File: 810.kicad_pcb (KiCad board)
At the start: 2 copper layers, 148 x 105.1 mm, 289 parts, among them J1 PJ301BM, J10 PJ301BM, J11 PJ301BM, J12 PJ301BM, J13 PJ301BM, J14 PJ301BM, J15 JACK_MONO_SW, J16 PJ301BM, J17 PJ301B, J18 PJ301B, J2 PJ301BM, J3 PJ301BM, J4 PJ301B, J5 PJ301B, J6 PJ301BM, J7 PJ301BM, J8 PJ301BM, J9 PJ301BM, P1 CONN_01X08, P2 CONN_02X05, Q1 PMBT2369, Q10 2SK208-GR, Q11 2SC4738, Q12 2SA1832, Q13 2SA1832, Q14 2SA1832, Q2 2SK208-GR, Q3 2SA1618, Q4 2SC4207, Q5 2SK208-GR, Q6 MMBF4391LT1G, Q7 2SA1832, Q8 PMBT2369, Q9 2SK208-GR, SW1 DP6T-QY-25S-A, SW1 SPDT, SW2 SPDT, SW3 BF3-1050, U1 TL072-, U10 RC4558, U11 TL074-, U12 TA75S558F, U13 TA75S558F, U14 TA75S558F, U15 TA75S558F, U16 TA75S558F, U17 CD4052, U18 TA75S558F, U2 TL072-, U3 TL072-, U4 CD40106, U5 CD4027, U6 LM13700, U7 LM13700, U8 LM13700, U9 TL072-

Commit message: added hard/soft sync switch
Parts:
- added P3: CONN_01X03, Pin_Headers:Pin_Header_Straight_1x03_Pitch2.54mm, F.Cu at (158.0, 161.2)
- added P4: CONN_01X08, Pin_Headers:Pin_Header_Angled_1x08_Pitch2.54mm, B.Cu at (104.8, 79.8)
- added R135: 15K, MyModules:SM0603-R-JRL, F.Cu at (158.0, 161.2)
- added SW4: SPDT, MyModules:SS-12F108-1P2T-SLIDE, F.Cu at (158.0, 161.2)
- C45, C46, D17, D18, F1, F2, P2: moved to B.Cu
- moved F1 111.9 mm to (223.2, 70.2), turned to 90 degrees
- moved C45 107.4 mm to (218.2, 72.2), turned to 90 degrees
- moved P2 104.8 mm to (226.5, 81.8)
- moved D17 104.3 mm to (212.2, 72.0), turned to 270 degrees
- moved F2 102.0 mm to (223.0, 82.5), turned to 270 degrees
- moved C46 100.6 mm to (218.2, 80.5), turned to 90 degrees
- moved D18 97.4 mm to (212.2, 80.2), turned to 270 degrees
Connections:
- D3 pad 2: -12V -> Net-(D3-Pad2)
- Q1 pad 2: -12V -> Net-(D3-Pad2)
- Q1 pad 3: SYNC -> Net-(Q1-Pad3)
- R8 pad 1: -12V -> Net-(D3-Pad2)

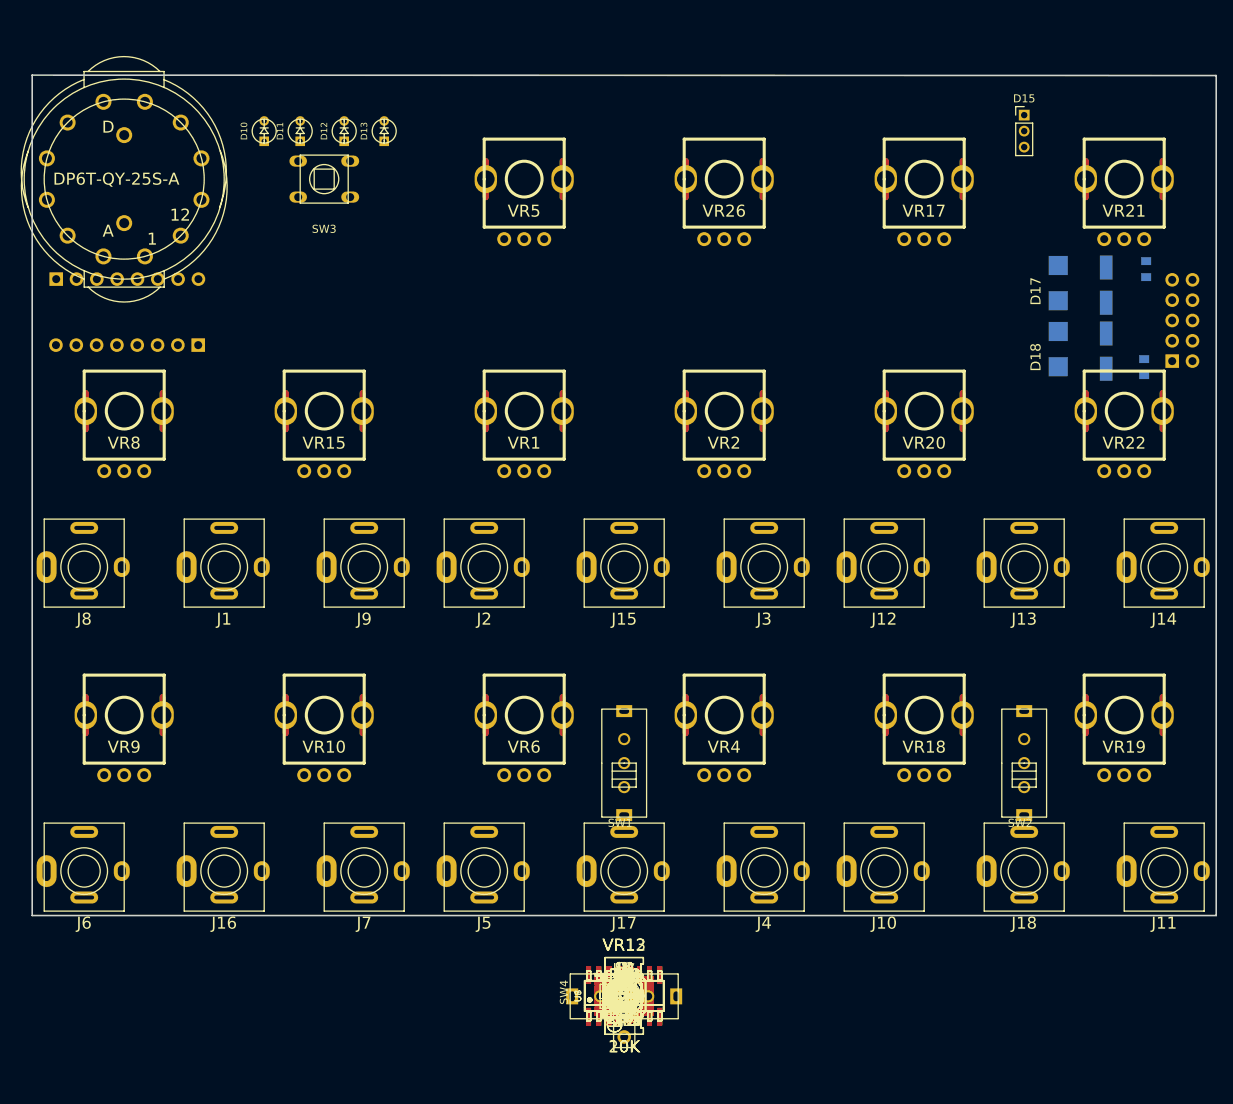
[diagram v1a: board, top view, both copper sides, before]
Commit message: updated SW1 rotary switch footprint to Alpha SR2511
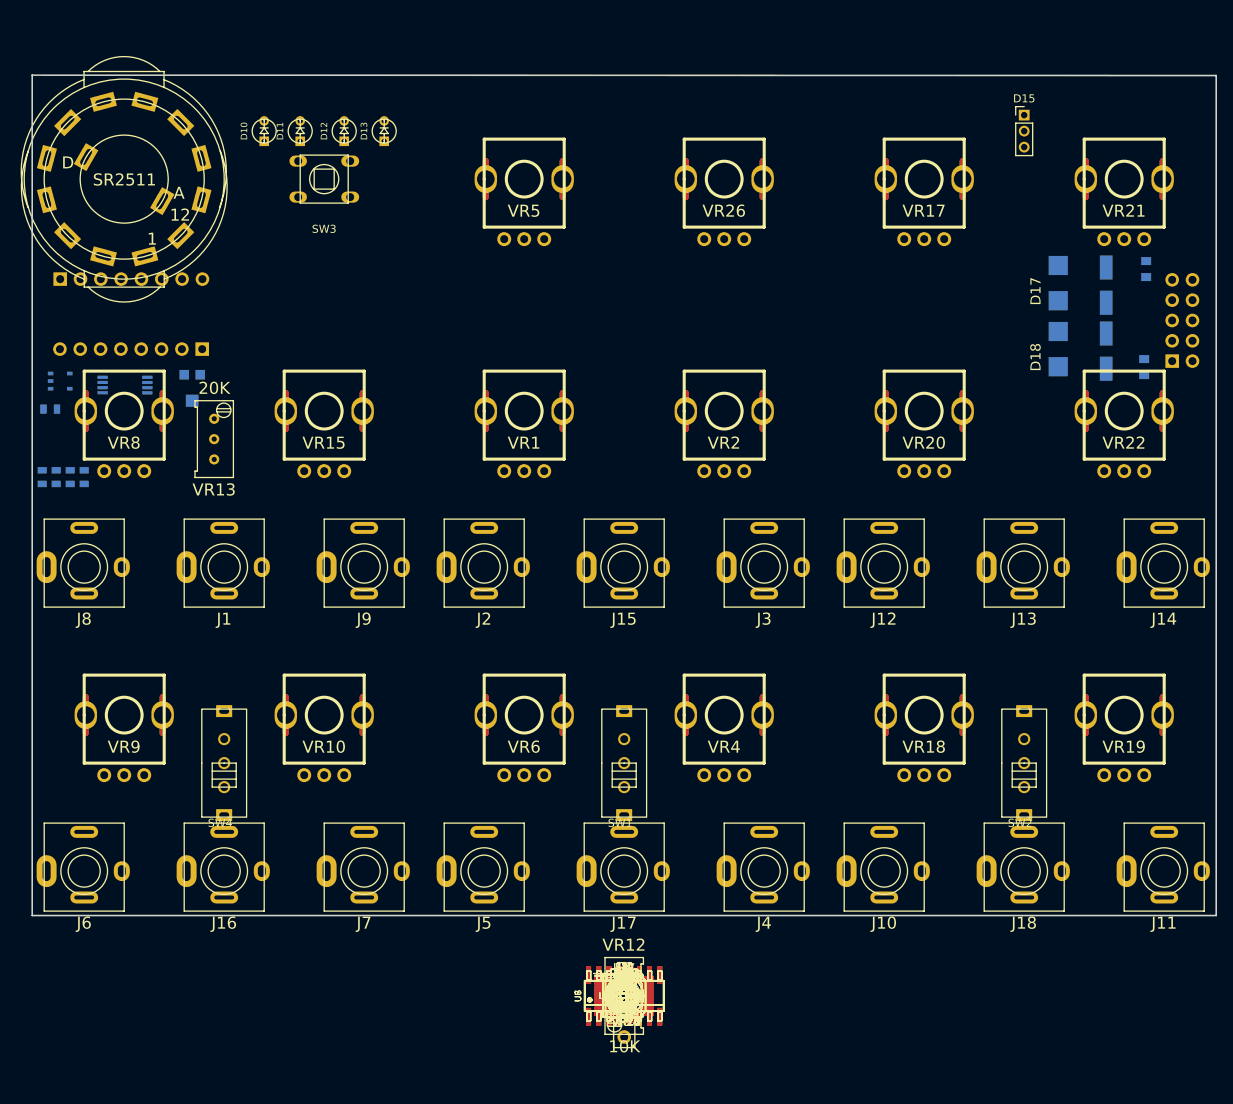
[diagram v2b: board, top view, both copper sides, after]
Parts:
- R27, R28, R29, R30, R31, U1, U13, VR3: moved to B.Cu
- SW1: value DP6T-QY-25S-A -> SR2511; footprint MyModules:QY-25S-2P6C-JRL -> MyModules:SR2511-ALPHA
- moved U13 104.3 mm to (87.5, 84.2)
- moved R27 102.6 mm to (86.2, 87.8)
- moved U1 98.7 mm to (95.5, 84.8), turned to 90 degrees
- moved R30 97.5 mm to (85.2, 96.2), turned to 90 degrees
- moved R28 96.2 mm to (87.0, 96.2), turned to 90 degrees
- moved R31 94.9 mm to (88.8, 96.2), turned to 90 degrees
- moved R29 93.6 mm to (90.5, 96.2), turned to 270 degrees
- moved VR3 93.1 mm to (104.0, 85.2)
- moved VR13 86.4 mm to (106.8, 91.5), turned to 180 degrees
- moved SW4 57.9 mm to (108.0, 132.0), turned to 90 degrees
- moved P1 20.2 mm to (105.2, 80.2), turned to 90 degrees
- moved P4 19.1 mm to (87.5, 71.5), turned to 270 degrees

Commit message: started PCB part placement
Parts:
- C1, C11, C12, C14, C17, C18, C33, C36, C9, D16, D3, D6, D7, D8, D9, P3, Q1, Q4, Q6, Q7, Q8, R102, R123, R125, R131, R132, R133, R134, R135, R37, R47, R49, R5, R51, R53, R57, R58, R60, R61, R62, R63, R66, R67, R68, R69, R71, R72, R8, R80, R82, R83, R84, R85, R86, R89, R90, R91, R95, R98, TC1, U15, U17, U2, U3, U4, U5, U6, U7, U8: moved to B.Cu
- P1, P4: footprint Pin_Headers:Pin_Header_Angled_1x08_Pitch2.54mm -> Pin_Headers:Pin_Header_Straight_1x08_Pitch2.54mm
- moved R134 107.5 mm to (124.5, 59.0), turned to 180 degrees
- moved U4 105.0 mm to (130.5, 59.8), turned to 90 degrees
- moved R123 102.4 mm to (116.5, 67.5), turned to 90 degrees
- moved D16 102.2 mm to (137.5, 61.0)
- moved R132 101.0 mm to (135.2, 62.8)
- moved U17 100.8 mm to (120.5, 67.5), turned to 270 degrees
- moved R133 100.3 mm to (138.2, 62.8)
- moved R37 98.4 mm to (93.5, 86.8), turned to 90 degrees
- moved C36 98.4 mm to (136.8, 65.0)
- moved R49 97.7 mm to (101.8, 81.2), turned to 90 degrees
- moved R66 97.6 mm to (104.0, 79.8), turned to 90 degrees
- moved R83 97.2 mm to (107.5, 78.0), turned to 180 degrees
- moved R47 97.1 mm to (95.5, 86.8), turned to 270 degrees
- moved R131 96.5 mm to (136.8, 67.0)
- moved C9 96.1 mm to (100.0, 84.5), turned to 180 degrees
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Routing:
- net Net-(R62-Pad2): track 0.00 -> 8.86 mm
- net Net-(R63-Pad1): track 0.00 -> 7.92 mm
- net Net-(C18-Pad1): track 0.00 -> 6.75 mm
- net Net-(R59-Pad2): track 0.00 -> 4.88 mm
- net Net-(D7-Pad2): track 0.00 -> 3.15 mm
- net Net-(C18-Pad2): track 0.00 -> 2.97 mm
- net Net-(R80-Pad1): track 0.00 -> 2.60 mm

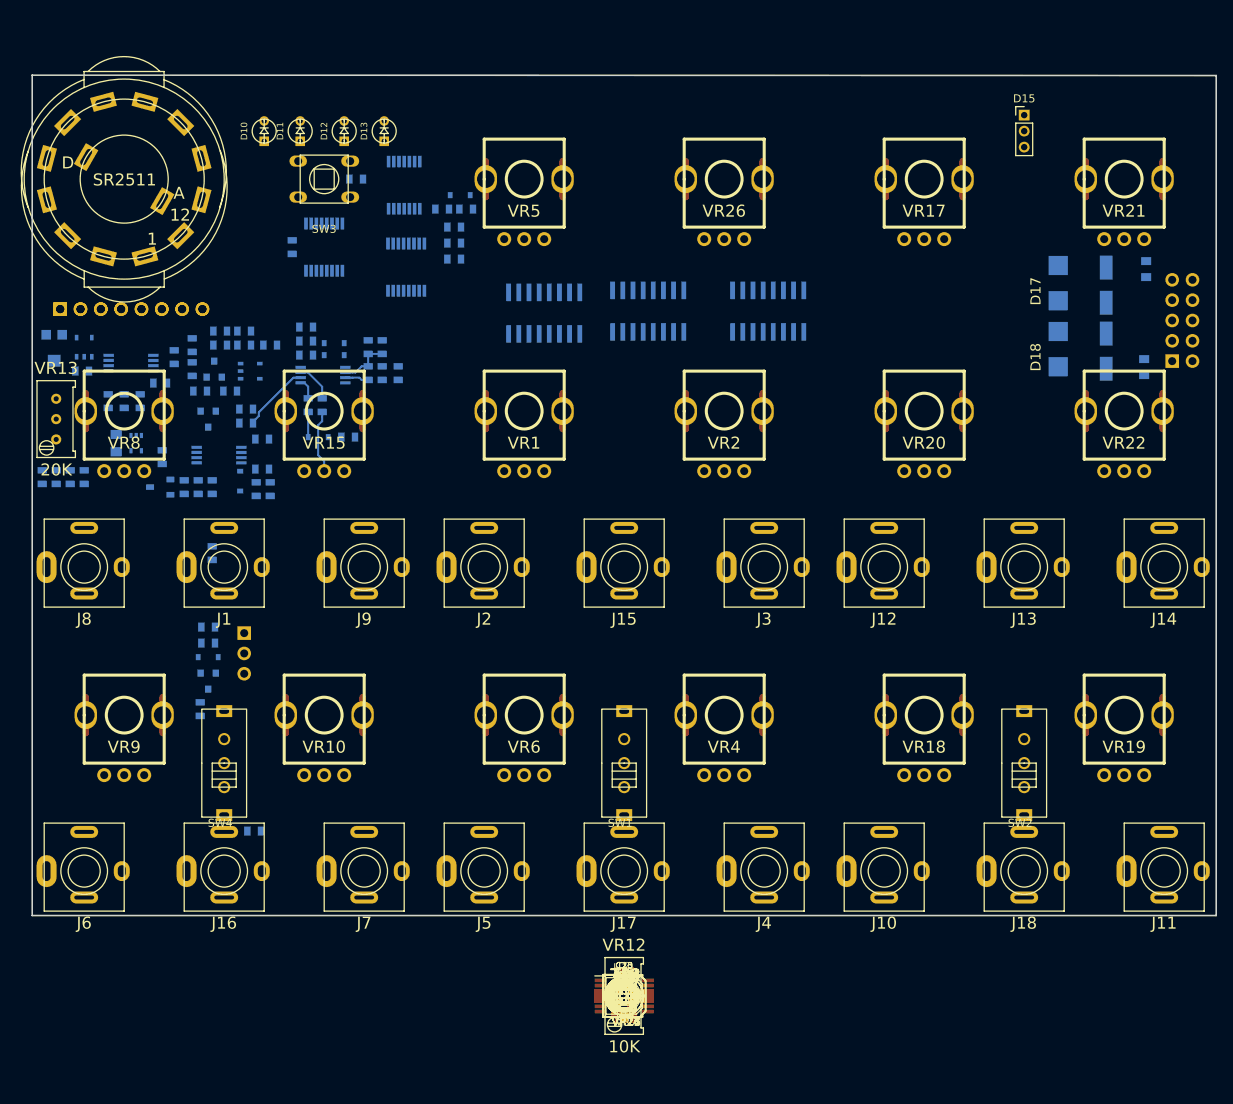
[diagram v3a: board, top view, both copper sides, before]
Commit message: more part placement. done VCO and VCF, started VCA
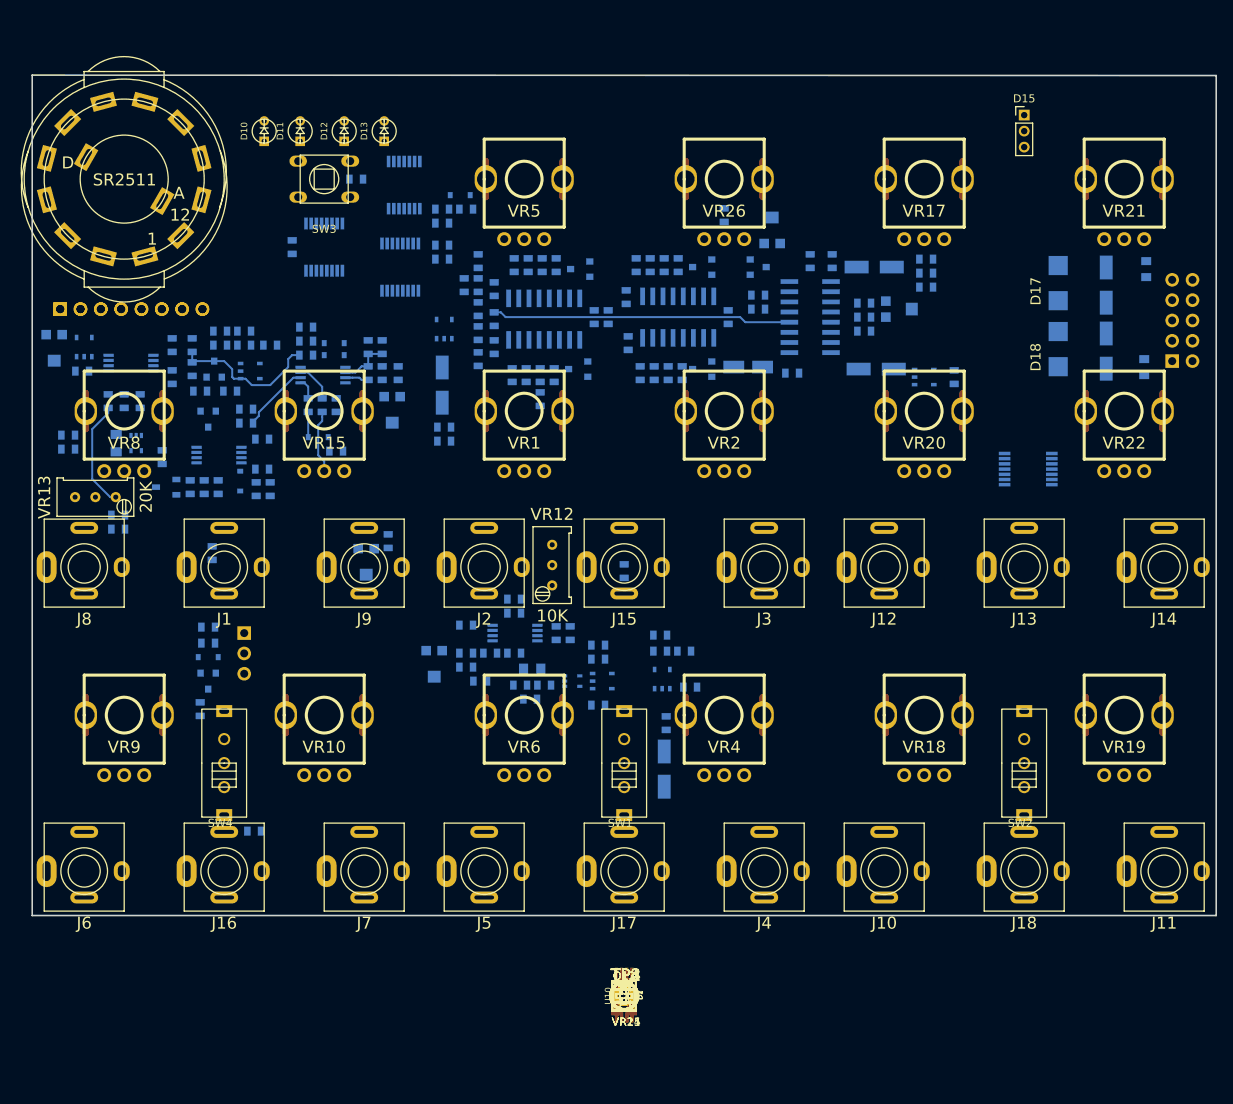
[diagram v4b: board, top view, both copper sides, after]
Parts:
- added R136: 47K, MyModules:SM0603-R-JRL, B.Cu at (181.2, 69.2)
- C10, C13, C15, C19, C2, C20, C21, C23, C24, C4, C5, C6, C8, Q10, Q14, Q2, Q3, Q5, Q9, R10, R101, R105, R106, R108, R109, R110, R111, R115, R121, R122, R124, R127, R129, R13, R14, R15, R16, R17, R18, R19, R20, R21, R22, R23, R24, R25, R26, R33, R34, R35, R36, R38, R39, R40, R41, R42, R43, R44, R45, R46, R48, R50, R52, R54, R55, R56, R59, R64, R65, R70, R74, R77, R78, R79, R81, R87, R9, R92, R93, R94, R97, U11, U12, U14, U16, U18, U9, VR14, VR16, VR23, VR27, VR7: moved to B.Cu
- C22: value 15p -> 22p
- moved R78 99.5 mm to (195.8, 69.0), turned to 180 degrees
- moved R121 98.4 mm to (170.5, 63.5), turned to 90 degrees
- moved R79 97.9 mm to (195.8, 70.8), turned to 180 degrees
- moved VR27 97.6 mm to (176.5, 65.2), turned to 180 degrees
- moved C15 96.3 mm to (189.2, 70.0), turned to 180 degrees
- moved R77 96.3 mm to (195.8, 72.5), turned to 180 degrees
- moved R105 95.5 mm to (184.0, 69.2), turned to 90 degrees
- moved R23 93.6 mm to (139.8, 69.2), turned to 270 degrees
- moved Q14 92.6 mm to (174.8, 70.0)
- moved VR23 92.5 mm to (192.5, 75.2), turned to 90 degrees
- moved R26 92.4 mm to (144.2, 69.8), turned to 270 degrees
- moved R39 92.1 mm to (146.0, 69.8), turned to 270 degrees
- moved R41 91.9 mm to (147.8, 69.8), turned to 90 degrees
- moved C6 91.7 mm to (149.5, 69.8), turned to 90 degrees
- moved R87 91.7 mm to (188.0, 74.5), turned to 180 degrees
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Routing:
- net Net-(R24-Pad2): track 0.00 -> 37.4 mm
- net Net-(Q8-Pad3): track 0.00 -> 18.7 mm
- net Net-(R37-Pad1): track 0.00 -> 13.6 mm

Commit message: added rotary switch, integrated into main PCB
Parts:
- C16, C22, C25, C26, C3, D1, D14, D2, D4, D5, Q11, Q12, Q13, R1, R100, R103, R104, R107, R11, R112, R113, R114, R116, R117, R118, R119, R12, R120, R126, R128, R130, R2, R3, R32, R4, R6, R7, R73, R75, R76, R88, R96, R99, U10, VR11, VR24, VR25: moved to B.Cu
- P4: moved to F.Cu
- SW5: renamed from SW1; value SR2511 -> DP6T-ALPHA-SR2511
- moved R116 129.9 mm to (230.0, 53.0), turned to 270 degrees
- moved R118 129.5 mm to (226.5, 51.2), turned to 90 degrees
- moved R126 129.5 mm to (222.8, 49.0), turned to 180 degrees
- moved R117 128.9 mm to (228.2, 53.0), turned to 90 degrees
- moved C26 127.7 mm to (219.2, 49.0)
- moved R119 126.9 mm to (226.5, 54.2), turned to 270 degrees
- moved R128 123.4 mm to (213.2, 50.8), turned to 270 degrees
- moved R120 122.8 mm to (215.2, 52.5), turned to 90 degrees
- moved R130 121.0 mm to (211.2, 52.5), turned to 270 degrees
- moved D14 120.9 mm to (219.0, 56.8)
- moved C25 120.3 mm to (213.2, 54.2), turned to 270 degrees
- moved R1 106.0 mm to (88.2, 81.2), turned to 180 degrees
- moved R2 104.1 mm to (91.2, 81.2), turned to 180 degrees
- moved R4 102.2 mm to (126.0, 64.0), turned to 90 degrees
- moved R6 102.2 mm to (94.2, 81.2), turned to 180 degrees
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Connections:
- P4 pad 7: Net-(P4-Pad7) -> Net-(P4-Pad6)
- SW5 pad 1: (no net) -> Net-(P4-Pad2)
- SW5 pad 10: (no net) -> Net-(P4-Pad5)
- SW5 pad 11: (no net) -> Net-(P4-Pad4)
- SW5 pad 12: (no net) -> Net-(P4-Pad3)
- SW5 pad 2: (no net) -> Net-(P4-Pad1)
- SW5 pad 9: (no net) -> Net-(P4-Pad6)
- SW5 pad A: (no net) -> Net-(P4-Pad8)
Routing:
- net Net-(P4-Pad6): track 0.00 -> 36.6 mm
- net Net-(P4-Pad5): track 0.00 -> 31.5 mm
- net Net-(P4-Pad8): track 0.00 -> 24.3 mm
- net Net-(P4-Pad4): track 0.00 -> 23.9 mm
- net Net-(C9-Pad1): track 0.00 -> 20.5 mm
- net Net-(P4-Pad3): track 0.00 -> 19.8 mm
- net Net-(P4-Pad1): track 0.00 -> 16.3 mm
- net Net-(D6-Pad2): track 0.00 -> 14.3 mm
- net Net-(P4-Pad2): track 0.00 -> 11.0 mm
- net Net-(C12-Pad2): track 0.00 -> 10.3 mm
- net Net-(Q8-Pad3): track 18.7 -> 9.02 mm
- net Net-(C9-Pad2): track 0.00 -> 7.81 mm
- net SYNC: track 0.00 -> 7.35 mm
- net Net-(Q4-Pad4): track 0.00 -> 7.27 mm
- net Net-(C12-Pad1): track 0.00 -> 4.90 mm
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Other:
- board size 148 x 105.1 mm -> 148 x 110.1 mm

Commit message: routing
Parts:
- C27, C28, C29, C30, C31, C32, C34, C35: moved to B.Cu
- moved C30 127.9 mm to (230.0, 50.0), turned to 90 degrees
- moved C29 126.2 mm to (228.2, 57.0), turned to 270 degrees
- moved C35 98.0 mm to (156.5, 69.8), turned to 270 degrees
- moved C32 84.6 mm to (182.5, 83.2), turned to 180 degrees
- moved C31 79.4 mm to (174.8, 78.2), turned to 180 degrees
- moved C3 79.1 mm to (138.0, 78.2), turned to 90 degrees
- moved C34 75.9 mm to (154.2, 79.2), turned to 90 degrees
- moved C28 71.5 mm to (203.5, 115.8)
- moved C27 69.4 mm to (213.0, 121.8)
- moved VR24 15.1 mm to (196.8, 129.8), turned to 270 degrees
- moved R105 14.0 mm to (183.8, 69.2), turned to 90 degrees
- moved R99 9.62 mm to (201.2, 129.0), turned to 180 degrees
- moved R75 8.84 mm to (209.0, 123.5), turned to 180 degrees
- moved R20 8.28 mm to (142.2, 107.5)
- moved R73 8.28 mm to (204.5, 125.5)
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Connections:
- VR11 pad 1: +10V -> -10V
- VR11 pad 3: -10V -> +10V
- VR7 pad 1: +10V -> -10V
- VR7 pad 3: -10V -> +10V
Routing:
- net -12V: track 0.00 -> 758.6 mm, vias 0 -> 31
- net +12V: track 0.00 -> 609.8 mm, vias 0 -> 23
- net +10V: track 0.00 -> 209.2 mm, vias 0 -> 5
- net (no net): track 136.1 -> 0.00 mm
- net VCO: track 0.00 -> 97.3 mm, vias 0 -> 1
- net Net-(R105-Pad2): track 0.00 -> 93.1 mm, vias 0 -> 1
- net Iabc: track 0.00 -> 86.3 mm, vias 0 -> 5
- net Net-(C21-Pad2): track 0.00 -> 75.8 mm, vias 0 -> 1
- net Net-(R73-Pad1): track 0.00 -> 65.1 mm, vias 0 -> 1
- net -10V: track 0.00 -> 64.2 mm, vias 0 -> 2
- net Net-(J18-Pad3): track 0.00 -> 59.9 mm, vias 0 -> 1
- net Net-(R106-Pad1): track 0.00 -> 52.0 mm, vias 0 -> 1
- net Net-(J4-Pad3): track 0.00 -> 50.8 mm, vias 0 -> 1
- net SYNC: track 7.35 -> 57.1 mm
- net Net-(R30-Pad1): track 0.00 -> 49.6 mm
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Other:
- outline, holes or cut-outs redrawn
- net class Default: via_dia 0.6 -> 0.8
- net class POWER added: clearance 0.2, trace_width 0.35, via_dia 0.9, via_drill 0.45
